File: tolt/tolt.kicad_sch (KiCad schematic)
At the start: 6 parts

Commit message: modified:   tolt/conn.kicad_sch 	modified:   tolt/powerstage.kicad_sch 	modified:   tolt/stm32.kicad_sch 	modified:   tolt/tolt.kicad_pcb 	modified:   tolt/tolt.kicad_pro 	modified:   tolt/tolt.kicad_sch
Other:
- sheet logic ports: added none; removed NRF_swclk, NRF_swdio
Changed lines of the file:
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@@
-			)
-		)
-		(pin "NRF_swclk" output
-			(at 117.348 153.924 270)
-			(effects
-				(font
-					(size 1.27 1.27)
-				)
-				(justify left)
-			)
-		)
-		(pin "NRF_swdio" bidirectional
-			(at 119.634 153.924 270)
-			(effects
-				(font
-					(size 1.27 1.27)
-				)
-				(justify left)
 			)
 		)

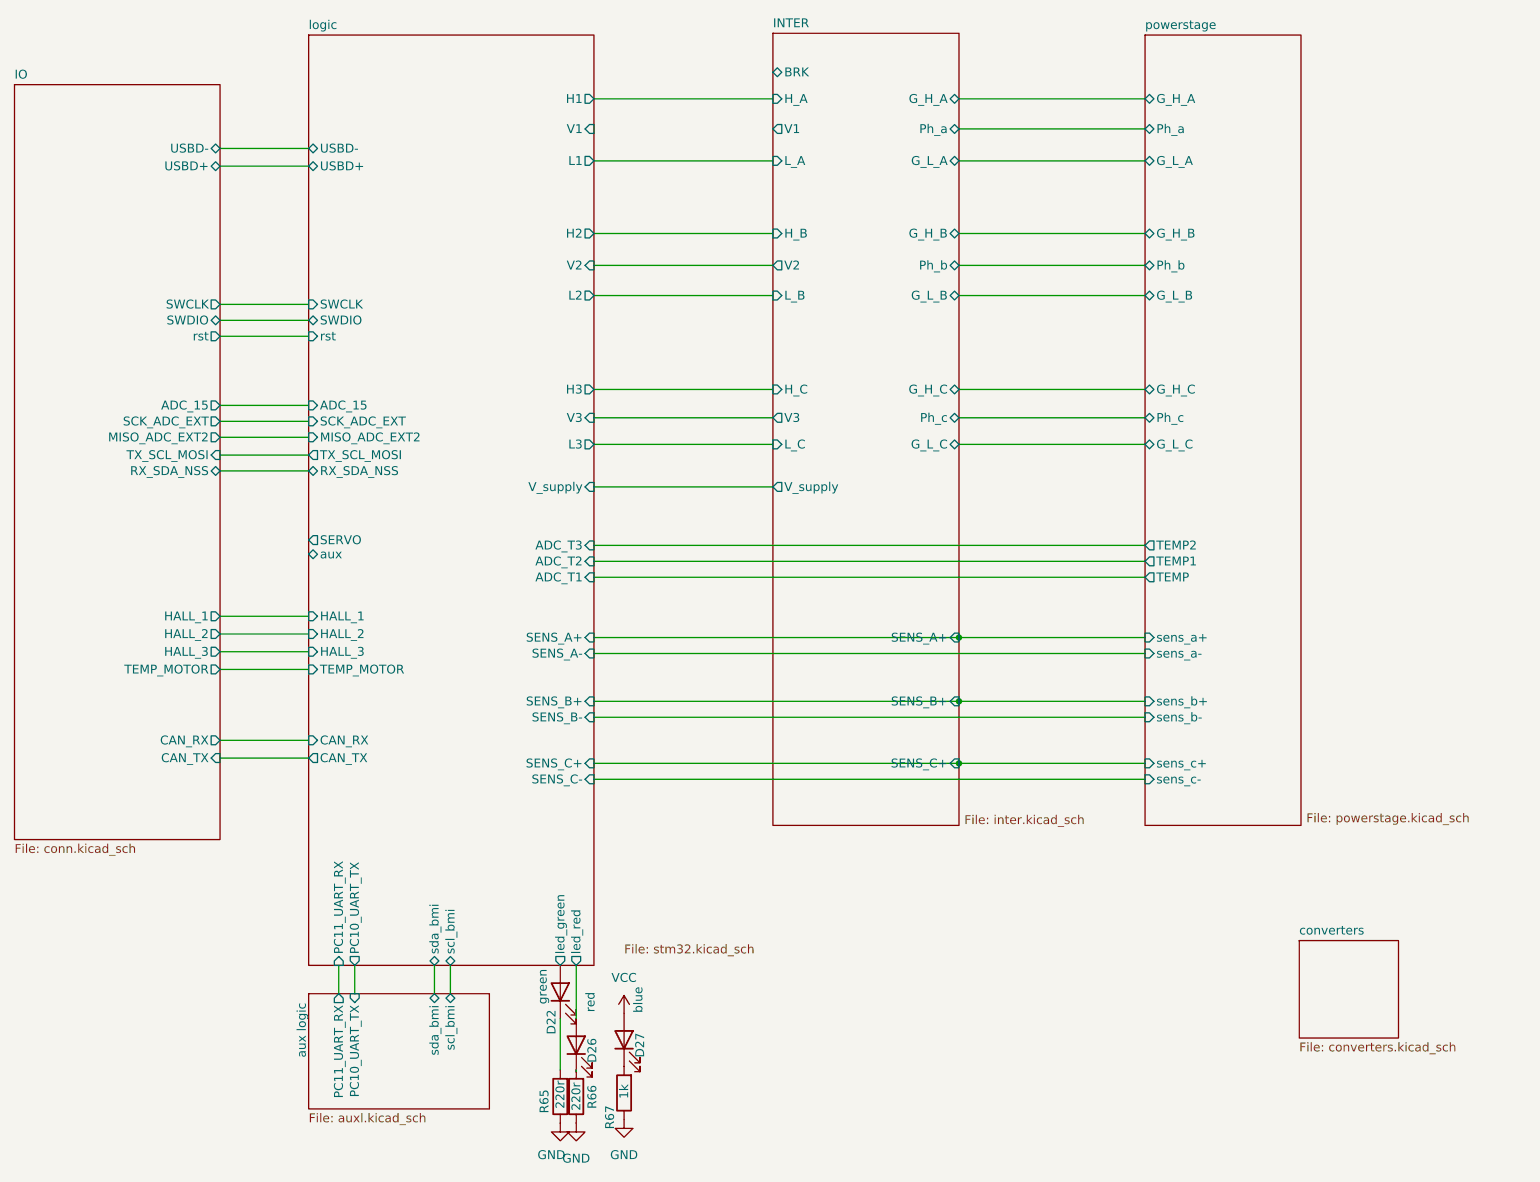
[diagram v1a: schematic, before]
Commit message: schem change
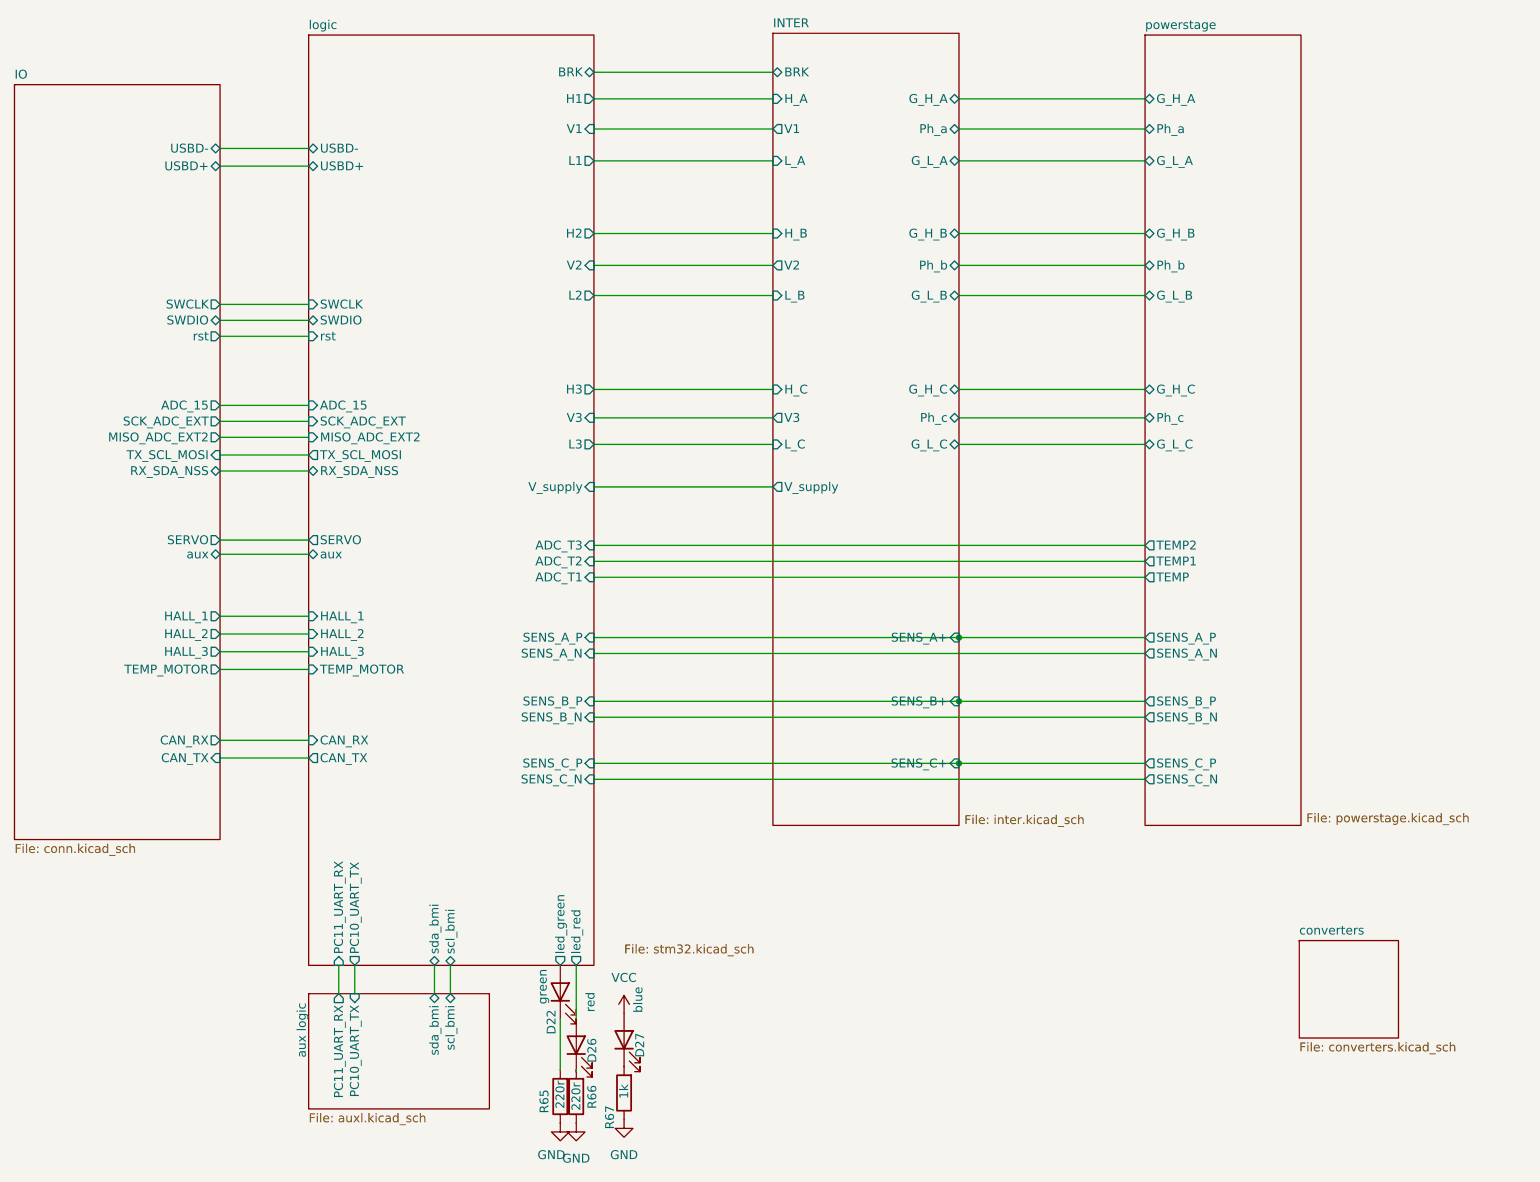
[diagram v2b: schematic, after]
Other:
- sheet IO ports: added SERVO, aux; removed none
- sheet logic ports: added BRK, SENS_A_N, SENS_A_P, SENS_B_N, SENS_B_P, SENS_C_N, SENS_C_P; removed SENS_A+, SENS_A-, SENS_B+, SENS_B-, SENS_C+, SENS_C-
- sheet powerstage ports: added SENS_A_N, SENS_A_P, SENS_B_N, SENS_B_P, SENS_C_N, SENS_C_P; removed sens_a+, sens_a-, sens_b+, sens_b-, sens_c+, sens_c-
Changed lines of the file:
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@@
+	(wire
+		(pts
+			(xy 95.758 94.996) (xy 108.458 94.996)
+		)
+		(stroke
+			(width 0)
+			(type default)
+		)
+	)
 	(wire
 		(pts
@@
 	(wire
 		(pts
+			(xy 95.758 92.964) (xy 108.458 92.964)
+		)
+		(stroke
+			(width 0)
+			(type default)
+		)
+	)
+	(wire
+		(pts
 			(xy 95.758 106.426) (xy 108.458 106.426)
 		)
@@
 	(wire
 		(pts
+			(xy 149.352 34.036) (xy 175.006 34.036)
+		)
+		(stroke
+			(width 0)
+			(type default)
+		)
+	)
+	(wire
+		(pts
 			(xy 95.758 36.83) (xy 108.458 36.83)
 		)
@@
 		(pts
 			(xy 95.758 61.468) (xy 108.458 61.468)
+		)
+		(stroke
+			(width 0)
+			(type default)
+		)
+	)
+	(wire
+		(pts
+			(xy 149.352 25.908) (xy 175.006 25.908)
 		)
 		(stroke
@@
 			)
 		)
-		(pin "SENS_A+" input
-			(at 149.352 106.934 0)
-			(effects
-				(font
-					(size 1.27 1.27)
-				)
-				(justify right)
-			)
-		)
-		(pin "SENS_A-" input
-			(at 149.352 109.22 0)
-			(effects
-				(font
-					(size 1.27 1.27)
-				)
-				(justify right)
-			)
-		)
-		(pin "SENS_B+" input
-			(at 149.352 116.078 0)
-			(effects
-				(font
-					(size 1.27 1.27)
-				)
-				(justify right)
-			)
-		)
-		(pin "SENS_B-" input
-			(at 149.352 118.364 0)
-			(effects
-				(font
-					(size 1.27 1.27)
-				)
-				(justify right)
-			)
-		)
-		(pin "SENS_C+" input
-			(at 149.352 124.968 0)
-			(effects
-				(font
-					(size 1.27 1.27)
-				)
-				(justify right)
-			)
-		)
-		(pin "SENS_C-" input
-			(at 149.352 127.254 0)
-			(effects
-				(font
-					(size 1.27 1.27)
-				)
-				(justify right)
-			)
-		)
 		(pin "SERVO" output
 			(at 108.458 92.964 180)
@@
 				)
 				(justify left)
+			)
+		)
+		(pin "SENS_A_N" input
+			(at 149.352 109.22 0)
+			(effects
+				(font
+					(size 1.27 1.27)
+				)
+				(justify right)
+			)
+		)
+		(pin "SENS_A_P" input
+			(at 149.352 106.934 0)
+			(effects
+				(font
+					(size 1.27 1.27)
+				)
+				(justify right)
+			)
+		)
+		(pin "SENS_B_N" input
+			(at 149.352 118.364 0)
+			(effects
+				(font
+					(size 1.27 1.27)
+				)
+				(justify right)
+			)
+		)
+		(pin "SENS_B_P" input
+			(at 149.352 116.078 0)
+			(effects
+				(font
+					(size 1.27 1.27)
+				)
+				(justify right)
+			)
+		)
+		(pin "SENS_C_N" input
+			(at 149.352 127.254 0)
+			(effects
+				(font
+					(size 1.27 1.27)
+				)
+				(justify right)
+			)
+		)
+		(pin "SENS_C_P" input
+			(at 149.352 124.968 0)
+			(effects
+				(font
+					(size 1.27 1.27)
+				)
+				(justify right)
+			)
+		)
+		(pin "BRK" bidirectional
+			(at 149.352 25.908 0)
+			(effects
+				(font
+					(size 1.27 1.27)
+				)
+				(justify right)
 			)
 		)
@@
 			)
 		)
+		(pin "aux" bidirectional
+			(at 95.758 94.996 0)
+			(effects
+				(font
+					(size 1.27 1.27)
+				)
+				(justify right)
+			)
+		)
+		(pin "SERVO" output
+			(at 95.758 92.964 0)
+			(effects
+				(font
+					(size 1.27 1.27)
+				)
+				(justify right)
+			)
+		)
 		(instances
 			(project "tolt"
@@
 			)
 		)
-		(pin "sens_a+" input
-			(at 228.346 106.934 180)
-			(effects
-				(font
-					(size 1.27 1.27)
-				)
-				(justify left)
-			)
-		)
-		(pin "sens_a-" input
-			(at 228.346 109.22 180)
-			(effects
-				(font
-					(size 1.27 1.27)
-				)
-				(justify left)
-			)
-		)
-		(pin "sens_b+" input
-			(at 228.346 116.078 180)
-			(effects
-				(font
-					(size 1.27 1.27)
-				)
-				(justify left)
-			)
-		)
-		(pin "sens_b-" input
-			(at 228.346 118.364 180)
-			(effects
-				(font
-					(size 1.27 1.27)
-				)
-				(justify left)
-			)
-		)
-		(pin "sens_c+" input
-			(at 228.346 124.968 180)
-			(effects
-				(font
-					(size 1.27 1.27)
-				)
-				(justify left)
-			)
-		)
-		(pin "sens_c-" input
-			(at 228.346 127.254 180)
-			(effects
-				(font
-					(size 1.27 1.27)
-				)
-				(justify left)
-			)
-		)
 		(pin "TEMP" output
 			(at 228.346 98.298 180)
@@
 			(effects
 				(font
+					(size 1.27 1.27)
+				)
+				(justify left)
+			)
+		)
+		(pin "SENS_A_N" output
+			(at 228.346 109.22 180)
+			(effects
+				(font
+					(size 1.27 1.27)
+				)
+				(justify left)
+			)
+		)
+		(pin "SENS_A_P" output
+			(at 228.346 106.934 180)
+			(effects
+				(font
+					(size 1.27 1.27)
+				)
+				(justify left)
+			)
+		)
+		(pin "SENS_B_N" output
+			(at 228.346 118.364 180)
+			(effects
+				(font
+					(size 1.27 1.27)
+				)
+				(justify left)
+			)
+		)
+		(pin "SENS_B_P" output
+			(at 228.346 116.078 180)
+			(effects
+				(font
+					(size 1.27 1.27)
+				)
+				(justify left)
+			)
+		)
+		(pin "SENS_C_N" output
+			(at 228.346 127.254 180)
+			(effects
+				(font
+					(size 1.27 1.27)
+				)
+				(justify left)
+			)
+		)
+		(pin "SENS_C_P" output
+			(at 228.346 124.968 180)
+			(effects
+				(font

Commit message: ltc
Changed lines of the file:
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@@
 	)
 	(sheet
-		(at 250.444 150.368)
-		(size 14.224 13.97)
+		(at 75.438 150.622)
+		(size 12.7 13.97)
 		(exclude_from_sim no)
 		(in_bom yes)
@@
 		)
 		(property "Sheetname" "converters"
-			(at 250.444 149.6564 0)
+			(at 75.438 149.9104 0)
 			(effects
 				(font
@@
 		)
 		(property "Sheetfile" "converters.kicad_sch"
-			(at 250.444 164.9226 0)
+			(at 75.438 165.1766 0)
 			(effects
 				(font

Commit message: begenning of lcsc part assign
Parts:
- D22, D26, D27: footprint Diode_SMD:D_0603_1608Metric_Pad1.05x0.95mm_HandSolder -> Diode_SMD:D_0603_1608Metric_Pad1.05x0.95mm
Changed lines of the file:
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@@
 			)
 		)
-		(property "Footprint" "Diode_SMD:D_0603_1608Metric_Pad1.05x0.95mm_HandSolder"
+		(property "Footprint" "Diode_SMD:D_0603_1608Metric_Pad1.05x0.95mm"
 			(at 146.812 165.354 0)
 			(effects
@@
 			)
 		)
-		(property "Footprint" "Diode_SMD:D_0603_1608Metric_Pad1.05x0.95mm_HandSolder"
+		(property "Footprint" "Diode_SMD:D_0603_1608Metric_Pad1.05x0.95mm"
 			(at 153.67 164.592 0)
 			(effects
@@
 			)
 		)
-		(property "Footprint" "Diode_SMD:D_0603_1608Metric_Pad1.05x0.95mm_HandSolder"
+		(property "Footprint" "Diode_SMD:D_0603_1608Metric_Pad1.05x0.95mm"
 			(at 144.526 157.734 0)
 			(effects

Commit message: more assign+12-5v change
changed with TPS82130
Since using esp32 will increase consumption by a lot
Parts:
- R67: LCSC (none) -> C2907114
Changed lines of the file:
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@@
+			)
+		)
+		(property "LCSC" "C2907114"
+			(at 153.67 172.212 90)
+			(effects
+				(font
+					(size 1.27 1.27)
+				)
+				(hide yes)
 			)
 		)

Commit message: hm
weird huh it didnt fucking save
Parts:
- D22: LCSC (none) -> C965804
- D26: LCSC (none) -> C965799
- D27: LCSC (none) -> C965807
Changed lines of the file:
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@@
+			)
+		)
+		(property "LCSC" "C965799"
+			(at 146.812 165.354 0)
+			(effects
+				(font
+					(size 1.27 1.27)
+				)
+				(hide yes)
 			)
 		)
@@
 		)
 		(property "Sim.Pins" "1=K 2=A"
+			(at 153.67 164.592 0)
+			(effects
+				(font
+					(size 1.27 1.27)
+				)
+				(hide yes)
+			)
+		)
+		(property "LCSC" "C965807"
 			(at 153.67 164.592 0)
 			(effects
@@
 			(at 144.526 157.734 0)
 			(effects
+				(font
+					(size 1.27 1.27)
+				)
+				(hide yes)
+			)
+		)
+		(property "LCSC" "C965804"
+			(at 144.526 157.734 0)
+			(effects

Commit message: Done
hopefully finished ?
needs sanity check and more checks
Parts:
- D22, D26, D27: footprint Diode_SMD:D_0603_1608Metric_Pad1.05x0.95mm -> LED_SMD:LED_0603_1608Metric
- R65, R66: LCSC (none) -> C107696
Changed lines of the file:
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@@
+			)
+		)
+		(property "LCSC" "C107696"
+			(at 146.812 172.72 90)
+			(effects
+				(font
+					(size 1.27 1.27)
+				)
+				(hide yes)
 			)
 		)
@@
 			)
 		)
+		(property "LCSC" "C107696"
+			(at 144.526 172.72 90)
+			(effects
+				(font
+					(size 1.27 1.27)
+				)
+				(hide yes)
+			)
+		)
 		(pin "1"
 		)
@@
 			)
 		)
-		(property "Footprint" "Diode_SMD:D_0603_1608Metric_Pad1.05x0.95mm"
+		(property "Footprint" "LED_SMD:LED_0603_1608Metric"
 			(at 146.812 165.354 0)
 			(effects
@@
 			)
 		)
-		(property "Footprint" "Diode_SMD:D_0603_1608Metric_Pad1.05x0.95mm"
+		(property "Footprint" "LED_SMD:LED_0603_1608Metric"
 			(at 153.67 164.592 0)
 			(effects
@@
 			)
 		)
-		(property "Footprint" "Diode_SMD:D_0603_1608Metric_Pad1.05x0.95mm"
+		(property "Footprint" "LED_SMD:LED_0603_1608Metric"
 			(at 144.526 157.734 0)
 			(effects

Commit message: fab
finally.
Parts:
- R67: LCSC C2907114 -> C22548
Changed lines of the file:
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@@
 			)
 		)
-		(property "LCSC" "C2907114"
+		(property "LCSC" "C22548"
 			(at 153.67 172.212 90)
 			(effects
